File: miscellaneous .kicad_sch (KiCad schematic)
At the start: 6 parts, among them J6 Conn_02x07_Odd_Even, U1 74LVC1G07SE-7, U2 74LVC1G07SE-7

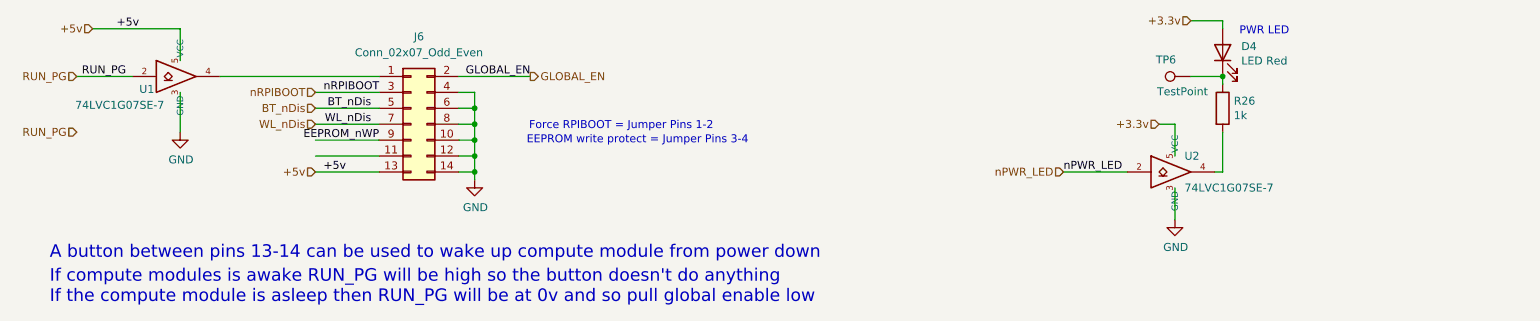
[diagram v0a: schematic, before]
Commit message: Redid traces with correct requirements, needs double checking.
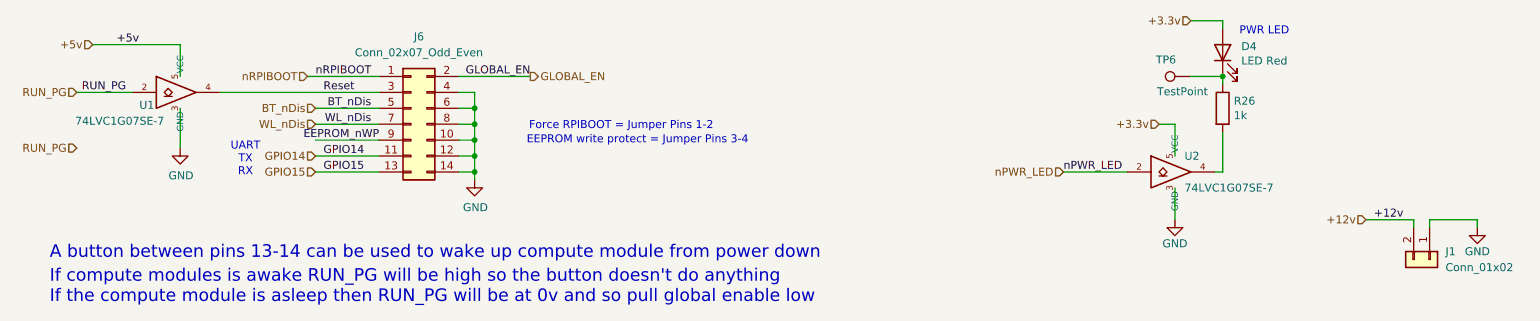
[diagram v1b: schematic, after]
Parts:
- added J1: Conn_01x02, Connector_PinHeader_2.54mm:PinHeader_1x02_P2.54mm_Vertical, symbol Connector_Generic:Conn_01x02
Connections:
- net +5v: no longer J6.13 (Pin_13)
- net GND: now also J1.1 (Pin_1)
- net nRPIBOOT: now also J6.1 (Pin_1); no longer J6.3 (Pin_3)
- net Reset: now reaches U1.4
- net Reset: now also J6.3 (Pin_3); no longer J6.1 (Pin_1)
- net GPIO14: now reaches J6.11 (Pin_11)
- new net +12v: J1.2 (Pin_2)
- new net GPIO15: J6.13 (Pin_13)
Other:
- note added: "UART TX RX"
- moved on the sheet: U1

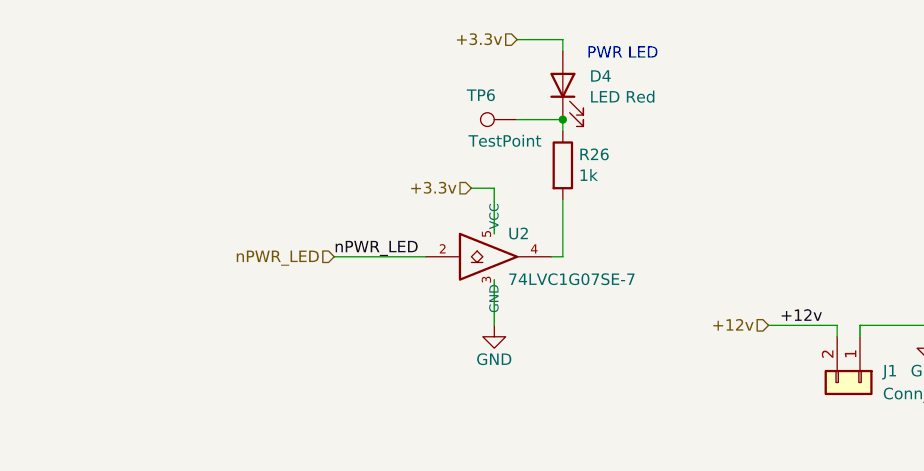
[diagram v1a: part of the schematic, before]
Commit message: Adjusted 3.3v for CM4 3.3v output, PCIe stayed the same.
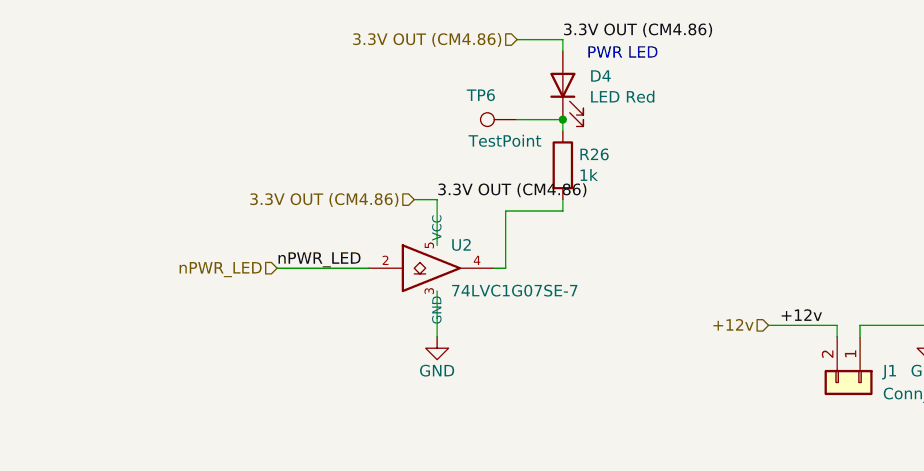
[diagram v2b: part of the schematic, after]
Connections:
- net +3.3v renamed 3.3V OUT (CM4.86)
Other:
- moved on the sheet: U2
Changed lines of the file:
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@@
 	(wire
 		(pts
-			(xy 201.93 45.72) (xy 201.93 50.8)
+			(xy 195.58 46.99) (xy 195.58 52.07)
 		)
 		(stroke
@@
 	(wire
 		(pts
-			(xy 201.93 40.64) (xy 201.93 35.56)
+			(xy 195.58 41.91) (xy 195.58 36.83)
 		)
 		(stroke
@@
 	(wire
 		(pts
+			(xy 203.2 38.1) (xy 209.55 38.1)
+		)
+		(stroke
+			(width 0)
+			(type solid)
+		)
+	)
+	(wire
+		(pts
 			(xy 87.63 35.56) (xy 90.17 35.56)
 		)
@@
 	(wire
 		(pts
-			(xy 184.15 43.18) (xy 194.31 43.18)
+			(xy 177.8 44.45) (xy 187.96 44.45)
 		)
 		(stroke
@@
 	(wire
 		(pts
-			(xy 209.55 43.18) (xy 208.28 43.18)
+			(xy 203.2 44.45) (xy 201.93 44.45)
 		)
 		(stroke
@@
 	(wire
 		(pts
-			(xy 201.93 35.56) (xy 199.39 35.56)
+			(xy 195.58 36.83) (xy 193.04 36.83)
 		)
 		(stroke
@@
 	(wire
 		(pts
-			(xy 209.55 36.83) (xy 209.55 43.18)
+			(xy 203.2 38.1) (xy 203.2 44.45)
 		)
 		(stroke
@@
 			(width 0)
 			(type default)
+		)
+	)
+	(wire
+		(pts
+			(xy 209.55 38.1) (xy 209.55 36.83)
+		)
+		(stroke
+			(width 0)
+			(type solid)
 		)
 	)
@@
 	)
 	(label "nPWR_LED"
-		(at 184.15 43.18 0)
+		(at 177.8 44.45 0)
 		(effects
 			(font
@@
 		)
 	)
+	(label "3.3V OUT (CM4.86)"
+		(at 209.55 19.05 0)
+		(effects
+			(font
+				(size 1.27 1.27)
+			)
+			(justify left bottom)
+		)
+	)
 	(label "+12v"
 		(at 233.68 50.8 0)
@@
 		)
 	)
+	(label "3.3V OUT (CM4.86)"
+		(at 195.58 36.83 0)
+		(effects
+			(font
+				(size 1.27 1.27)
+			)
+			(justify left bottom)
+		)
+	)
 	(label "GPIO14"
 		(at 66.04 40.64 0)
@@
 		)
 	)
-	(hierarchical_label "+3.3v"
+	(hierarchical_label "3.3V OUT (CM4.86)"
 		(shape input)
-		(at 199.39 35.56 180)
+		(at 193.04 36.83 180)
 		(effects
 			(font
@@
 	(hierarchical_label "nPWR_LED"
 		(shape input)
-		(at 184.15 43.18 180)
+		(at 177.8 44.45 180)
 		(effects
 			(font
@@
 		)
 	)
-	(hierarchical_label "+3.3v"
+	(hierarchical_label "3.3V OUT (CM4.86)"
 		(shape input)
 		(at 204.47 19.05 180)
@@
 	(symbol
 		(lib_id "CM4IO:74LVC1G07_copy")
-		(at 201.93 43.18 0)
+		(at 195.58 44.45 0)
 		(unit 1)
 		(exclude_from_sim no)
@@
 		(dnp no)
 		(property "Reference" "U2"
-			(at 203.454 40.64 0)
+			(at 197.104 41.91 0)
 			(effects
 				(font
@@
 		)
 		(property "Value" "74LVC1G07SE-7"
-			(at 203.454 45.72 0)
+			(at 197.104 46.99 0)
 			(effects
 				(font
@@
 		)
 		(property "Footprint" "Package_TO_SOT_SMD:SOT-353_SC-70-5"
-			(at 201.93 43.18 0)
+			(at 195.58 44.45 0)
 			(effects
 				(font
@@
 		)
 		(property "Datasheet" "https://www.diodes.com/assets/Datasheets/74LVC1G07.pdf"
-			(at 201.93 43.18 0)
+			(at 195.58 44.45 0)
 			(effects
 				(font
@@
 		)
 		(property "Description" ""
-			(at 201.93 43.18 0)
+			(at 195.58 44.45 0)
 			(effects
 				(font
@@
 		)
 		(property "Field4" "Farnell"
-			(at 201.93 43.18 0)
+			(at 195.58 44.45 0)
 			(effects
 				(font
@@
 		)
 		(property "Field5" "2425492"
-			(at 201.93 43.18 0)
+			(at 195.58 44.45 0)
 			(effects
 				(font
@@
 		)
 		(property "Field6" "74LVC1G07SE-7"
-			(at 201.93 43.18 0)
+			(at 195.58 44.45 0)
 			(effects
 				(font
@@
 		)
 		(property "Field7" "Diodes"
-			(at 201.93 43.18 0)
+			(at 195.58 44.45 0)
 			(effects
 				(font
@@
 		)
 		(property "Part Description" "Buffer, Non-Inverting 1 Element 1 Bit per Element Open Drain Output SOT-353"
-			(at 201.93 43.18 0)
+			(at 195.58 44.45 0)
 			(effects
 				(font
@@
 	(symbol
 		(lib_id "power:GND")
-		(at 201.93 50.8 0)
+		(at 195.58 52.07 0)
 		(unit 1)
 		(exclude_from_sim no)
@@
 		(dnp no)
 		(property "Reference" "#PWR012"
-			(at 201.93 57.15 0)
+			(at 195.58 58.42 0)
 			(effects
 				(font
@@
 		)
 		(property "Value" "GND"
-			(at 201.93 54.61 0)
+			(at 195.58 55.88 0)
 			(effects
 				(font
@@
 		)
 		(property "Footprint" ""
-			(at 201.93 50.8 0)
+			(at 195.58 52.07 0)
 			(effects
 				(font
@@
 		)
 		(property "Datasheet" ""
-			(at 201.93 50.8 0)
+			(at 195.58 52.07 0)
 			(effects
 				(font
@@
 		)
 		(property "Description" ""
-			(at 201.93 50.8 0)
-			(effects
-				(font
+			(at 195.58 52.07 0)
+			(effects
+				(font

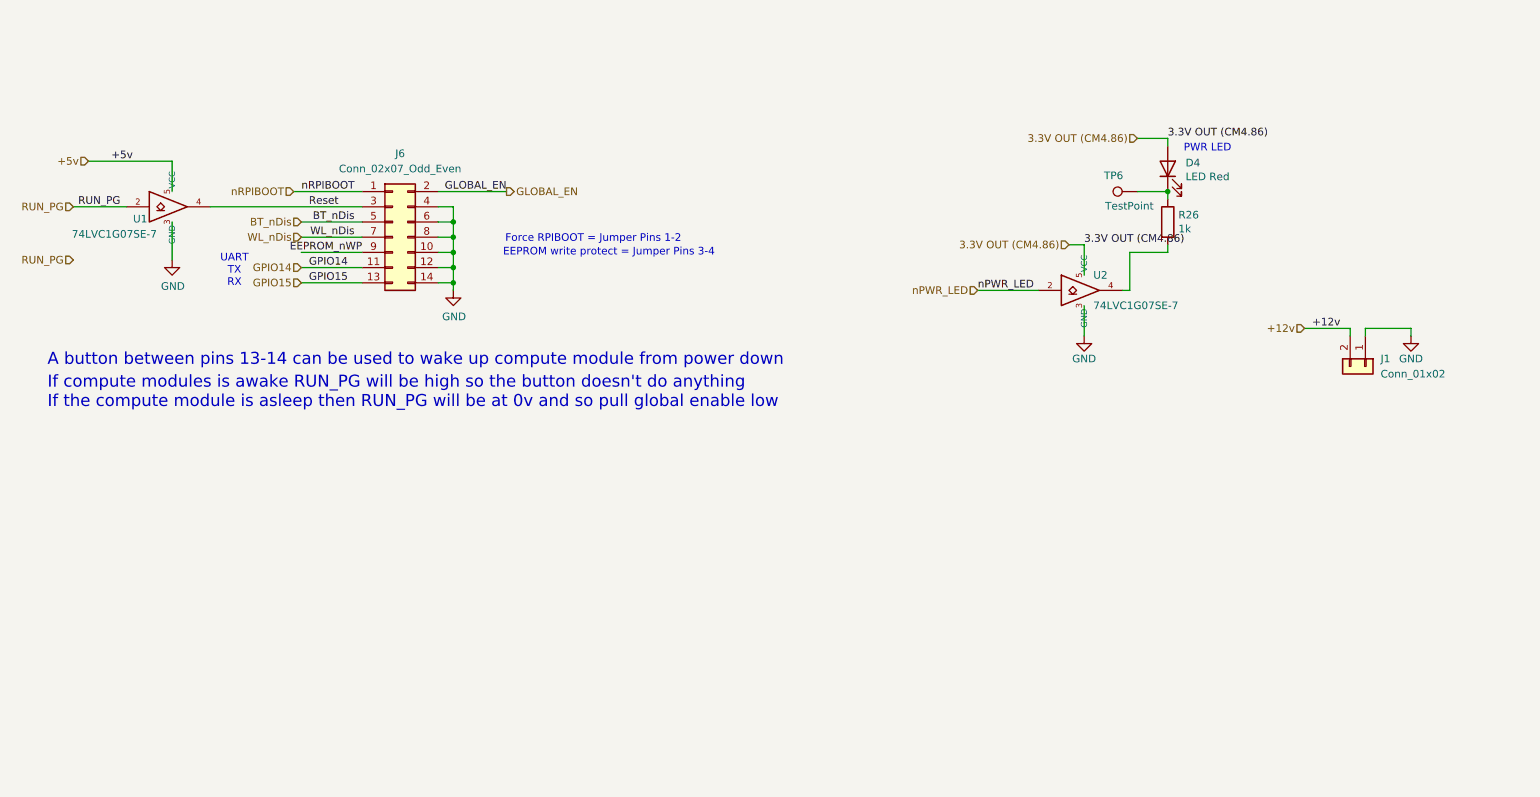
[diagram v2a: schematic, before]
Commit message: Changed quite a bit, PCB smoll now
Redid all traces, replaced HUSB238 with ch224k, made PCB even smaller.
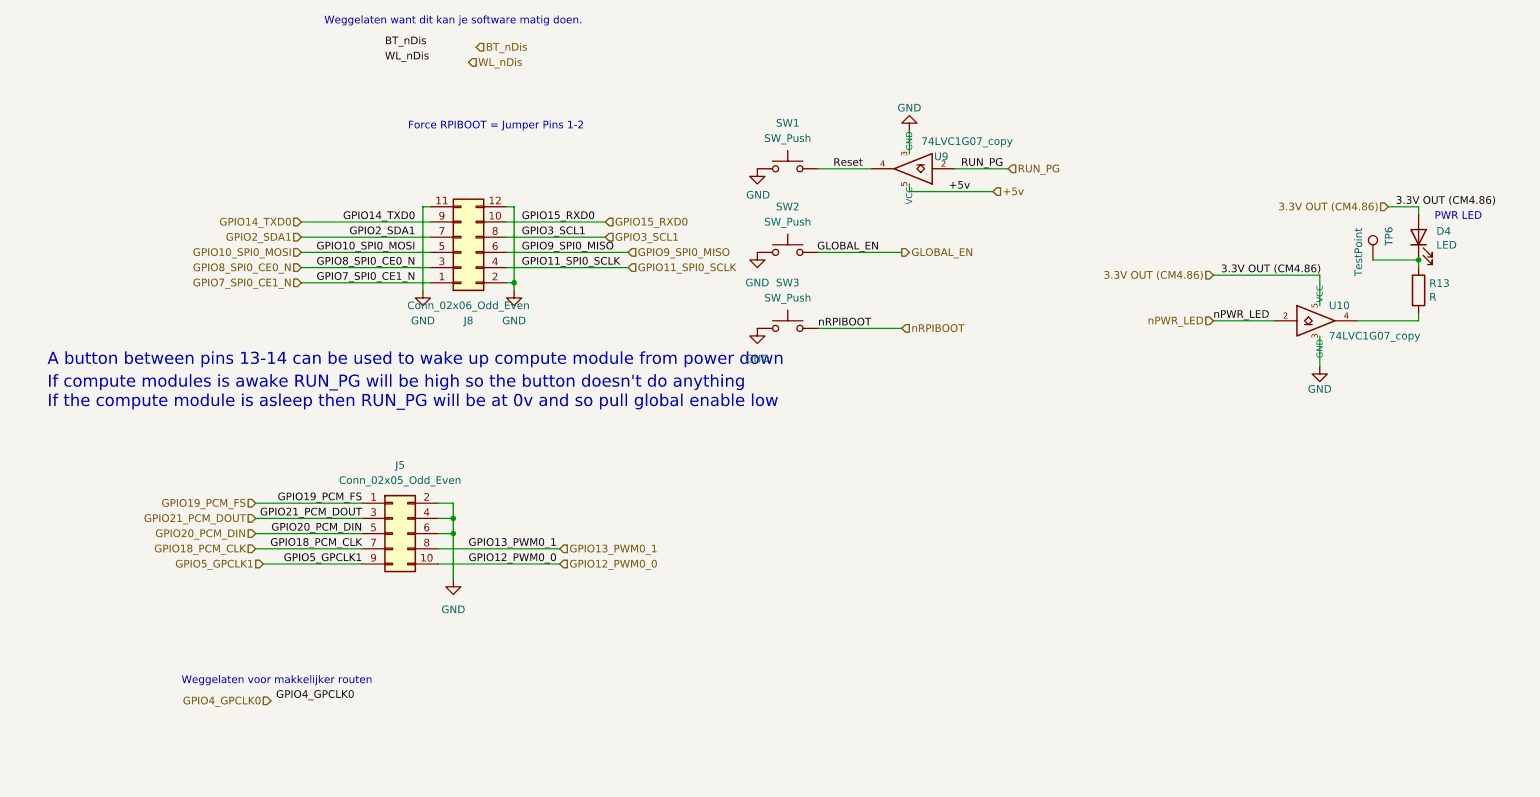
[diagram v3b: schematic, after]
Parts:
- removed J1: Conn_01x02, Connector_PinHeader_2.54mm:PinHeader_1x02_P2.54mm_Vertical, symbol Connector_Generic:Conn_01x02
- removed J6: Conn_02x07_Odd_Even, Connector_PinHeader_2.54mm:PinHeader_2x07_P2.54mm_Vertical, symbol Connector_Generic:Conn_02x07_Odd_Even
- added J5: Conn_02x05_Odd_Even, Connector_PinHeader_2.54mm:PinHeader_2x05_P2.54mm_Vertical, symbol Connector_Generic:Conn_02x05_Odd_Even
- added J8: Conn_02x06_Odd_Even, Connector_PinHeader_2.54mm:PinHeader_2x06_P2.54mm_Vertical, symbol Connector_Generic:Conn_02x06_Odd_Even
- added SW1, SW2, SW3: SW_Push, Button_Switch_SMD:SW_SPST_TS-1088-xR020, symbol Switch:SW_Push
- D4: value LED Red -> LED
- R13: renamed from R26; value 1k -> R
- U10: renamed from U2; value 74LVC1G07SE-7 -> 74LVC1G07_copy
- U9: renamed from U1; value 74LVC1G07SE-7 -> 74LVC1G07_copy
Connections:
- net GLOBAL_EN: now also SW2.2
- net GND: now also J5.2 (Pin_2), J5.4 (Pin_4), J5.6 (Pin_6), J8.11 (Pin_11), J8.12 (Pin_12), J8.2 (Pin_2), SW1.1, SW2.1, SW3.1
- net Reset: now also SW1.2
- net nRPIBOOT: now also SW3.2
- new net GPIO10_SPI0_MOSI: J8.5 (Pin_5)
- new net GPIO11_SPI0_SCLK: J8.4 (Pin_4)
- new net GPIO12_PWM0_0: J5.10 (Pin_10)
- new net GPIO13_PWM0_1: J5.8 (Pin_8)
- new net GPIO14_TXD0: J8.9 (Pin_9)
- new net GPIO15_RXD0: J8.10 (Pin_10)
- new net GPIO18_PCM_CLK: J5.7 (Pin_7)
- new net GPIO19_PCM_FS: J5.1 (Pin_1)
- new net GPIO20_PCM_DIN: J5.5 (Pin_5)
- new net GPIO21_PCM_DOUT: J5.3 (Pin_3)
- new net GPIO2_SDA1: J8.7 (Pin_7)
- new net GPIO3_SCL1: J8.8 (Pin_8)
- new net GPIO5_GPCLK1: J5.9 (Pin_9)
- new net GPIO7_SPI0_CE1_N: J8.1 (Pin_1)
- new net GPIO8_SPI0_CE0_N: J8.3 (Pin_3)
- new net GPIO9_SPI0_MISO: J8.6 (Pin_6)
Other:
- note added: "Weggelaten voor makkelijker routen"
- note added: "Weggelaten want dit kan je software matig doen."
- note removed: "EEPROM write protect = Jumper Pins 3-4"
- note removed: "UART TX RX"
- moved on the sheet: D4, R13, TP6, U10, U9

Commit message: Added datasheets for to-be-ordered components, double checked BOM
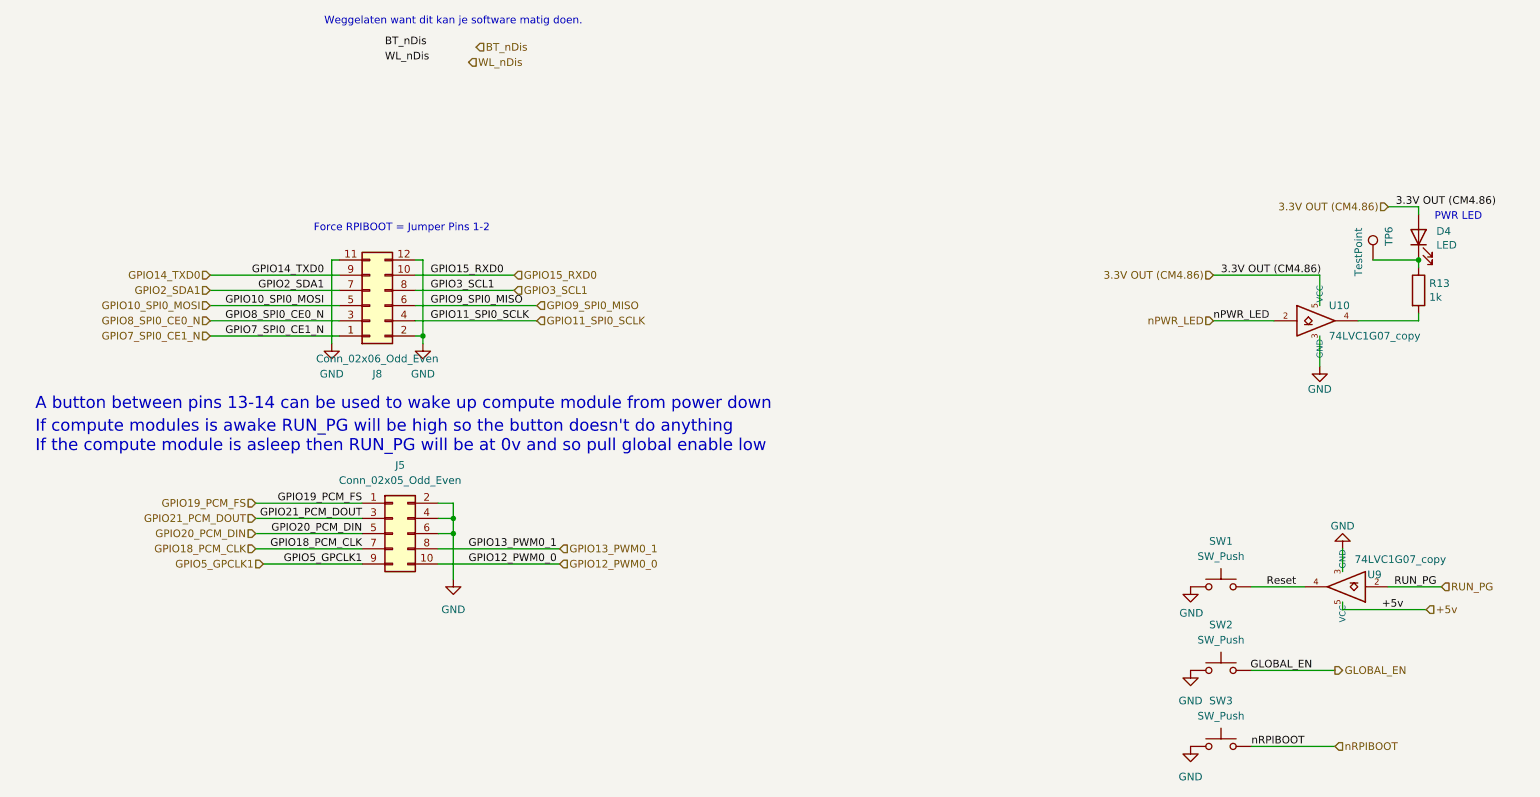
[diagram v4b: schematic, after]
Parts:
- R13: value R -> 1k
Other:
- note removed: "Weggelaten voor makkelijker routen"
- moved on the sheet: J8, SW1, SW2, SW3, U9
